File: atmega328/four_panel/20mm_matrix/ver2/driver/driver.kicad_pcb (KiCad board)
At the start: 2 copper layers, 40 x 40 mm, 56 parts, among them IC1 ATMEGA328P-M, IC2 ATMEGA328P-M, IC3 ATMEGA328P-M, IC4 ATMEGA328P-M, P1 CONN_2X2, P2 CONN_2X2, P3 CONN_2X2, P4 CONN_2X2, X1 CER_RESO, X2 CER_RESO, X3 CER_RESO, X4 CER_RESO

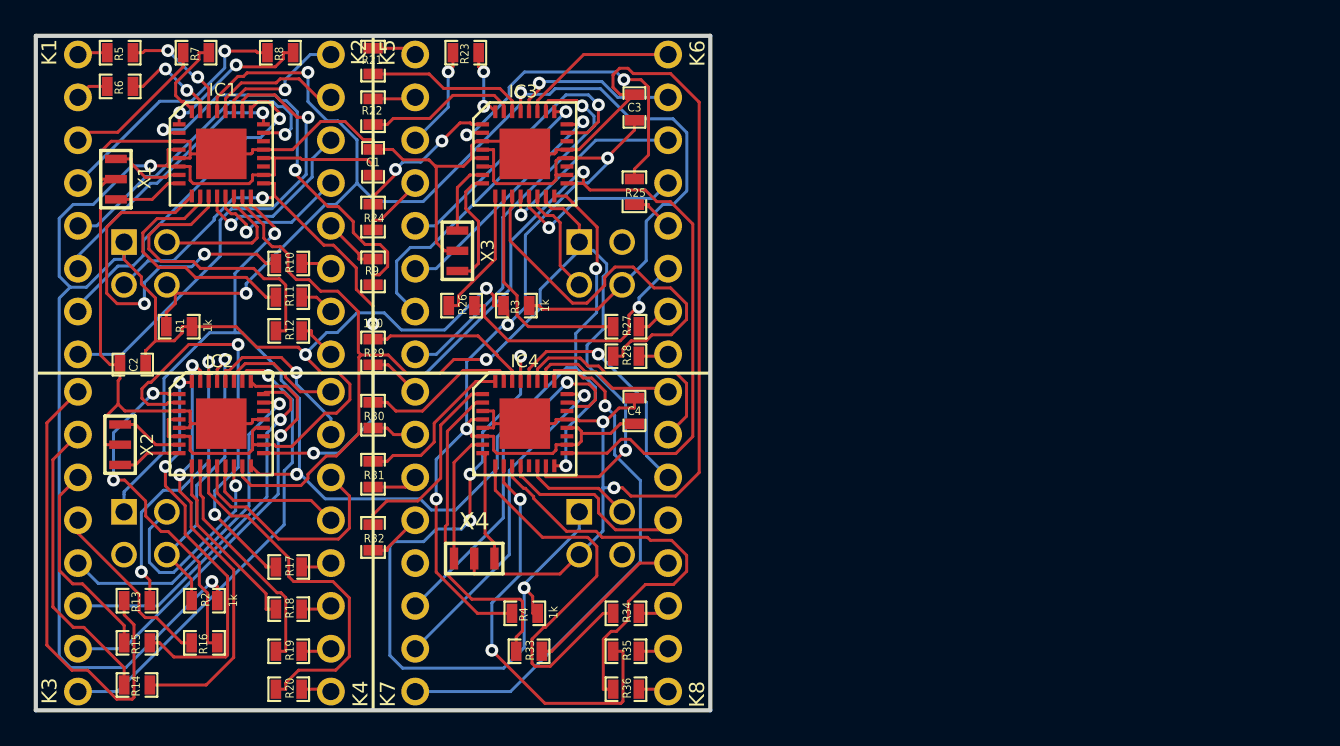
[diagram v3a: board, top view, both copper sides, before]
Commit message: Added new driver programmer for 4x20mm atmega328 driver.  Fixed issue with resistors and LED matrices on driver, then re-routed the board.
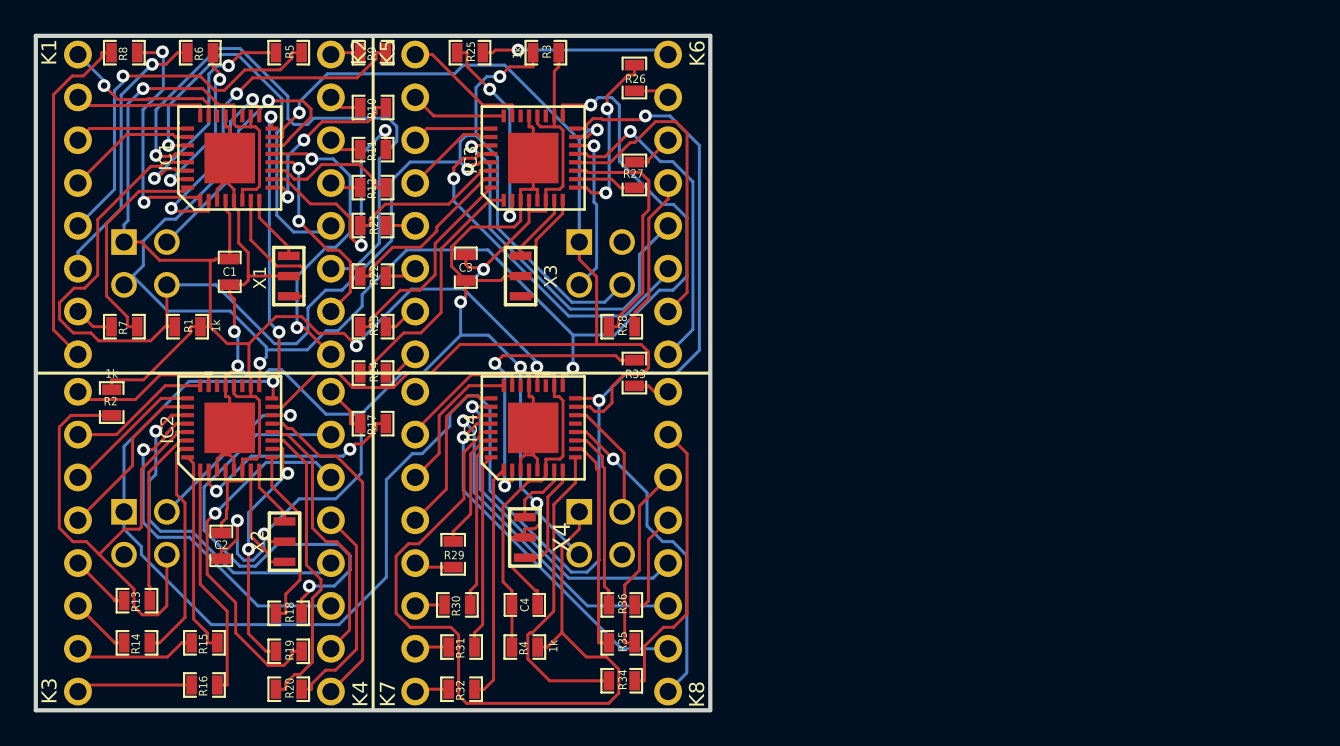
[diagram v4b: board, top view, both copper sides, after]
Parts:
- moved R33 17.6 mm to (85.5, 70.0), turned to 270 degrees
- moved R23 17.2 mm to (70.0, 67.2), turned to 0 degrees
- moved R26 17.0 mm to (85.5, 52.5), turned to 270 degrees
- moved R7 16.8 mm to (55.2, 67.2)
- moved R3 15.1 mm to (80.2, 51.0), turned to 0 degrees
- moved C3 13.8 mm to (75.5, 63.8), turned to 270 degrees
- moved C4 13.2 mm to (79.0, 83.8), turned to 0 degrees
- moved R9 13.0 mm to (70.0, 51.0), turned to 180 degrees
- moved R2 13.0 mm to (54.5, 71.8), turned to 90 degrees
- moved R29 12.9 mm to (74.8, 80.8)
- moved R25 12.8 mm to (75.8, 51.0), turned to 0 degrees
- moved R30 12.3 mm to (75.0, 83.8), turned to 180 degrees
- moved C2 12.0 mm to (61.0, 80.2), turned to 270 degrees
- moved X1 11.8 mm to (65.0, 64.2), turned to 90 degrees
- moved R31 11.5 mm to (75.2, 86.2), turned to 180 degrees
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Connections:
- MATRIX1 pad 1: N-0000094 -> /COL0_DRV0
- MATRIX1 pad 10: N-0000080 -> /COL6_DRV0
- MATRIX1 pad 11: N-0000079 -> /COL5_DRV0
- MATRIX1 pad 12: N-0000078 -> /COL4_DRV0
- MATRIX1 pad 13: /COL7_DRV0 -> N-0000081
- MATRIX1 pad 14: /COL6_DRV0 -> N-0000080
- MATRIX1 pad 15: /COL5_DRV0 -> N-0000079
- MATRIX1 pad 16: /COL4_DRV0 -> N-0000078
- MATRIX1 pad 2: N-0000095 -> /COL1_DRV0
- MATRIX1 pad 3: N-0000096 -> /COL2_DRV0
- MATRIX1 pad 4: N-0000077 -> /COL3_DRV0
- MATRIX1 pad 5: /COL0_DRV0 -> N-0000094
- MATRIX1 pad 6: /COL1_DRV0 -> N-0000095
- MATRIX1 pad 7: /COL2_DRV0 -> N-0000096
- MATRIX1 pad 8: /COL3_DRV0 -> N-0000077
- MATRIX1 pad 9: N-0000081 -> /COL7_DRV0
- MATRIX2 pad 1: N-00000109 -> /COL0_DRV1
- MATRIX2 pad 10: N-00000105 -> /COL6_DRV1
- MATRIX2 pad 11: N-00000104 -> /COL5_DRV1
- MATRIX2 pad 12: N-00000112 -> /COL4_DRV1
- MATRIX2 pad 13: /COL7_DRV1 -> N-00000106
- MATRIX2 pad 14: /COL6_DRV1 -> N-00000105
- MATRIX2 pad 15: /COL5_DRV1 -> N-00000104
- MATRIX2 pad 16: /COL4_DRV1 -> N-00000112
- MATRIX2 pad 2: N-00000107 -> /COL1_DRV1
- MATRIX2 pad 3: N-00000108 -> /COL2_DRV1
- MATRIX2 pad 4: N-00000110 -> /COL3_DRV1
- MATRIX2 pad 5: /COL0_DRV1 -> N-00000109
- MATRIX2 pad 6: /COL1_DRV1 -> N-00000107
- MATRIX2 pad 7: /COL2_DRV1 -> N-00000108
- MATRIX2 pad 8: /COL3_DRV1 -> N-00000110
- MATRIX2 pad 9: N-00000106 -> /COL7_DRV1
- MATRIX3 pad 1: N-00000111 -> /COL0_DRV2
- MATRIX3 pad 10: N-00000118 -> /COL6_DRV2
- MATRIX3 pad 11: N-00000117 -> /COL5_DRV2
- MATRIX3 pad 12: N-00000116 -> /COL4_DRV2
- MATRIX3 pad 13: /COL7_DRV2 -> N-00000119
- MATRIX3 pad 14: /COL6_DRV2 -> N-00000118
- MATRIX3 pad 15: /COL5_DRV2 -> N-00000117
- MATRIX3 pad 16: /COL4_DRV2 -> N-00000116
- MATRIX3 pad 2: N-00000114 -> /COL1_DRV2
- MATRIX3 pad 3: N-00000115 -> /COL2_DRV2
- MATRIX3 pad 4: N-00000113 -> /COL3_DRV2
- MATRIX3 pad 5: /COL0_DRV2 -> N-00000111
- MATRIX3 pad 6: /COL1_DRV2 -> N-00000114
- MATRIX3 pad 7: /COL2_DRV2 -> N-00000115
- MATRIX3 pad 8: /COL3_DRV2 -> N-00000113
- MATRIX3 pad 9: N-00000119 -> /COL7_DRV2
- MATRIX4 pad 1: N-0000087 -> /COL0_DRV3
- MATRIX4 pad 10: N-0000044 -> /COL6_DRV3
- MATRIX4 pad 11: N-0000045 -> /COL5_DRV3
- MATRIX4 pad 12: N-0000046 -> /COL4_DRV3
- MATRIX4 pad 13: /COL7_DRV3 -> N-0000044
- MATRIX4 pad 14: /COL6_DRV3 -> N-0000045
- MATRIX4 pad 15: /COL5_DRV3 -> N-0000046
- MATRIX4 pad 16: /COL4_DRV3 -> N-0000047
- MATRIX4 pad 2: N-0000083 -> /COL1_DRV3
- MATRIX4 pad 3: N-0000085 -> /COL2_DRV3
- MATRIX4 pad 4: N-0000089 -> /COL3_DRV3
- MATRIX4 pad 5: /COL0_DRV3 -> N-0000087
- MATRIX4 pad 6: /COL1_DRV3 -> N-0000083
- MATRIX4 pad 7: /COL2_DRV3 -> N-0000085
- MATRIX4 pad 8: /COL3_DRV3 -> N-0000089
- MATRIX4 pad 9: N-0000043 -> /COL7_DRV3
- R33 pad 2: N-0000046 -> N-0000047
- R34 pad 2: N-0000045 -> N-0000046
- R35 pad 2: N-0000044 -> N-0000045
- R36 pad 2: N-0000043 -> N-0000044
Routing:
- net +5V: track 189.2 -> 130.5 mm, vias 8 -> 4
- net /MISO: track 79.0 -> 119.8 mm, vias 4 -> 5
- net /COL5_DRV0: track 7.97 -> 34.3 mm, vias 0 -> 1
- net N-00000104: track 1.82 -> 27.2 mm, vias 0 -> 1
- net N-00000109: track 28.3 -> 3.71 mm
- net /COL3_DRV3: track 31.7 -> 10.1 mm, vias 1 -> 0
- net N-0000094: track 1.78 -> 22.1 mm, vias 0 -> 1
- net GND: track 141.2 -> 121.0 mm, vias 2 -> 7
- net /COL3_DRV0: track 27.9 -> 7.75 mm, vias 1 -> 0
- net N-00000105: track 1.80 -> 21.7 mm, vias 0 -> 1
- net /COL3_DRV1: track 28.1 -> 10.2 mm, vias 1 -> 0
- net /COL3_DRV2: track 23.1 -> 5.75 mm, vias 1 -> 0
- net /COL2_DRV1: track 25.0 -> 8.44 mm, vias 1 -> 0
- net /COL4_DRV0: track 7.94 -> 23.4 mm
- net N-0000095: track 2.01 -> 16.3 mm, vias 0 -> 1
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
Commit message: Adde ground holes to 4x20mm atmega328 comm
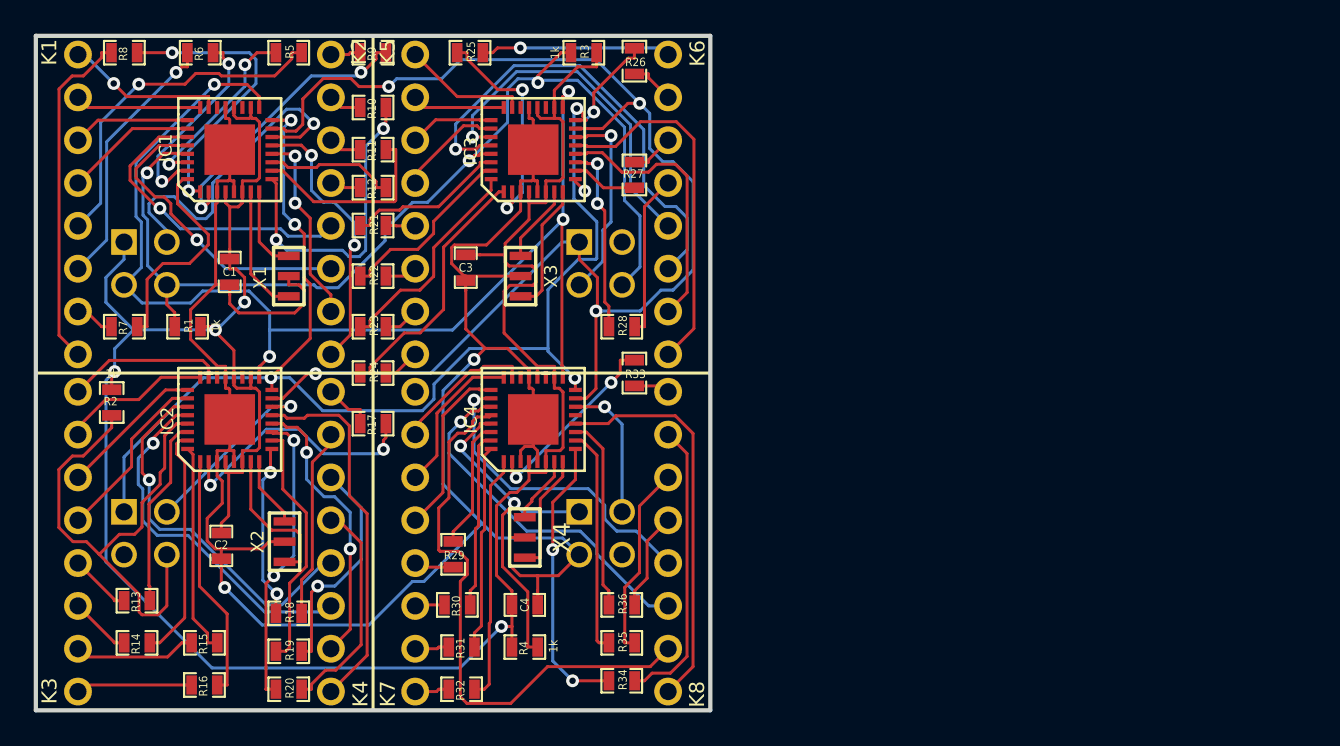
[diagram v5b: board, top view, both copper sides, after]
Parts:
- moved R3 2.25 mm to (82.5, 51.0)
- moved R26 1.00 mm to (85.5, 51.5)
- moved IC1 0.50 mm to (61.5, 56.8)
- moved IC2 0.50 mm to (61.5, 72.8)
- moved IC3 0.50 mm to (79.5, 56.8)
- moved IC4 0.50 mm to (79.5, 72.8)
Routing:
- net /MISO: track 119.8 -> 73.6 mm
- net /RESET_DRV3: track 46.7 -> 21.3 mm, vias 0 -> 2
- net /COL5_DRV0: track 34.3 -> 18.3 mm
- net N-00000104: track 27.2 -> 11.3 mm, vias 1 -> 0
- net +5V: track 130.5 -> 145.9 mm
- net /RESET_DRV0: track 78.1 -> 62.8 mm, vias 2 -> 3
- net /COL6_DRV3: track 21.2 -> 34.0 mm, vias 1 -> 0
- net /MOSI: track 69.6 -> 81.4 mm, vias 2 -> 4
- net /SCK: track 79.1 -> 70.4 mm
- net N-00000105: track 21.7 -> 13.5 mm
- net /ROW5_DRV0: track 11.0 -> 18.5 mm
- net GND: track 121.0 -> 128.4 mm, vias 7 -> 2
- net /COL5_DRV2: track 21.4 -> 28.0 mm
- net /ROW4_DRV3: track 17.3 -> 11.4 mm
- net /COL4_DRV0: track 23.4 -> 18.5 mm
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
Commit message: Re-routed 4x20mm atmega328 driver - modified clock traces.
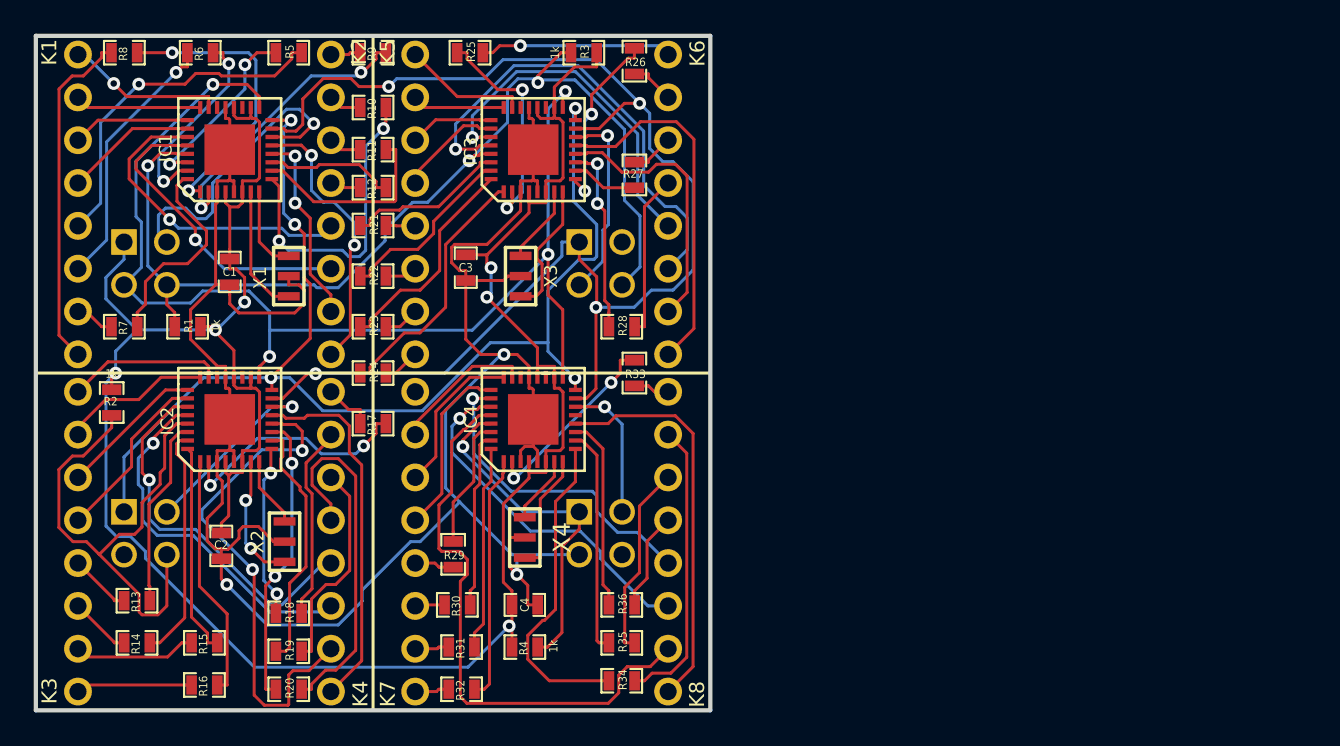
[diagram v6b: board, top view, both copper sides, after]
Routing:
- net /COL6_DRV1: track 16.9 -> 30.1 mm
- net N-00000106: track 13.2 -> 21.5 mm
- net +5V: track 145.9 -> 142.4 mm, vias 4 -> 6
- net /ROW5_DRV3: track 16.9 -> 19.0 mm, vias 2 -> 0
- net /CS0: track 20.1 -> 18.3 mm
- net /MISO: track 73.6 -> 72.2 mm
- net /SCK: track 70.4 -> 69.2 mm
- net /XTAL0_DRV1: track 8.91 -> 7.73 mm, vias 0 -> 2
- net /ROW4_DRV1: track 15.4 -> 14.5 mm
- net GND: track 128.4 -> 127.6 mm, vias 2 -> 3
- net N-00000105: track 13.5 -> 12.6 mm, vias 1 -> 0
- net /RESET_DRV3: track 21.3 -> 20.5 mm, vias 2 -> 1
